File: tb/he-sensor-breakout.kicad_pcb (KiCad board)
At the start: 2 copper layers, 19 x 19 mm, 24 parts, among them J1 Conn_01x01_Pin, J10 Conn_01x01_Pin, J11 Conn_01x01_Pin, J12 Conn_01x01_Pin, J13 Conn_01x01_Pin, J14 Conn_01x01_Pin, J2 Conn_01x01_Pin, J3 Conn_01x01_Pin, J4 Conn_01x01_Pin, J5 Conn_01x01_Pin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

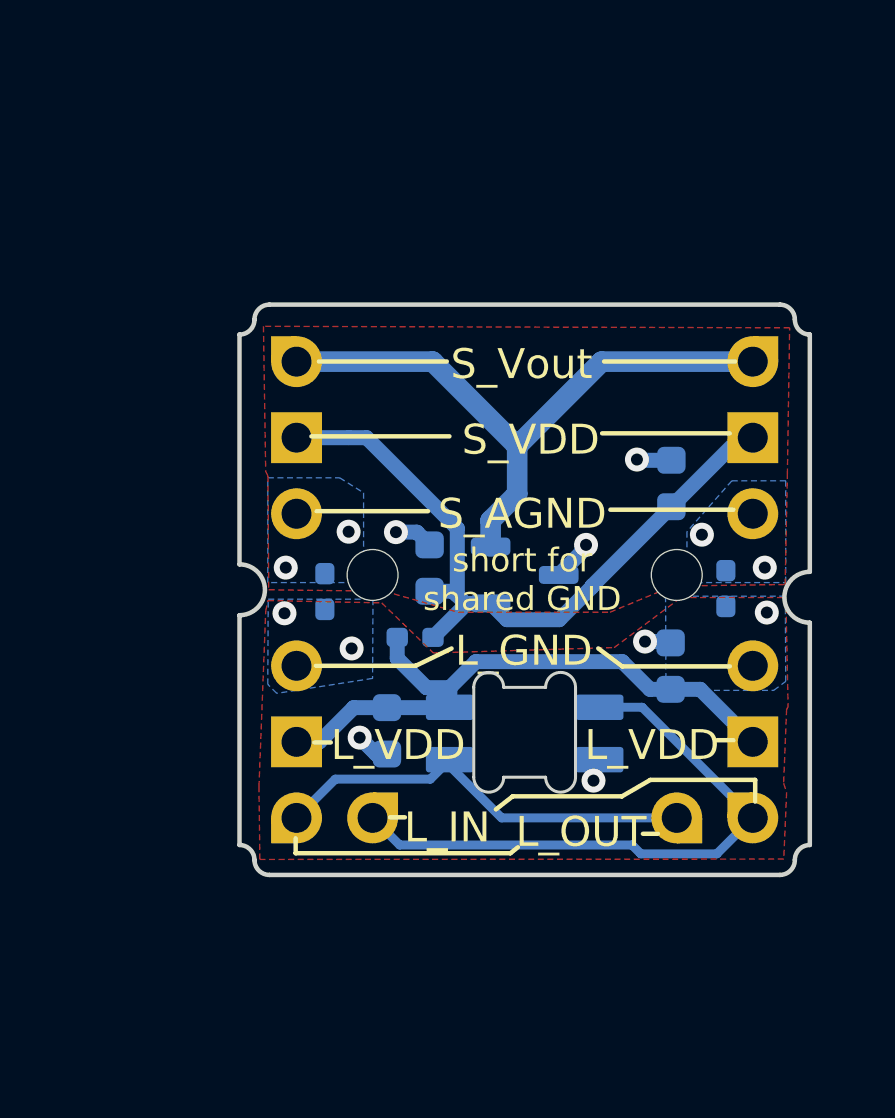
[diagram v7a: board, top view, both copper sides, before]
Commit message: fix screw hole
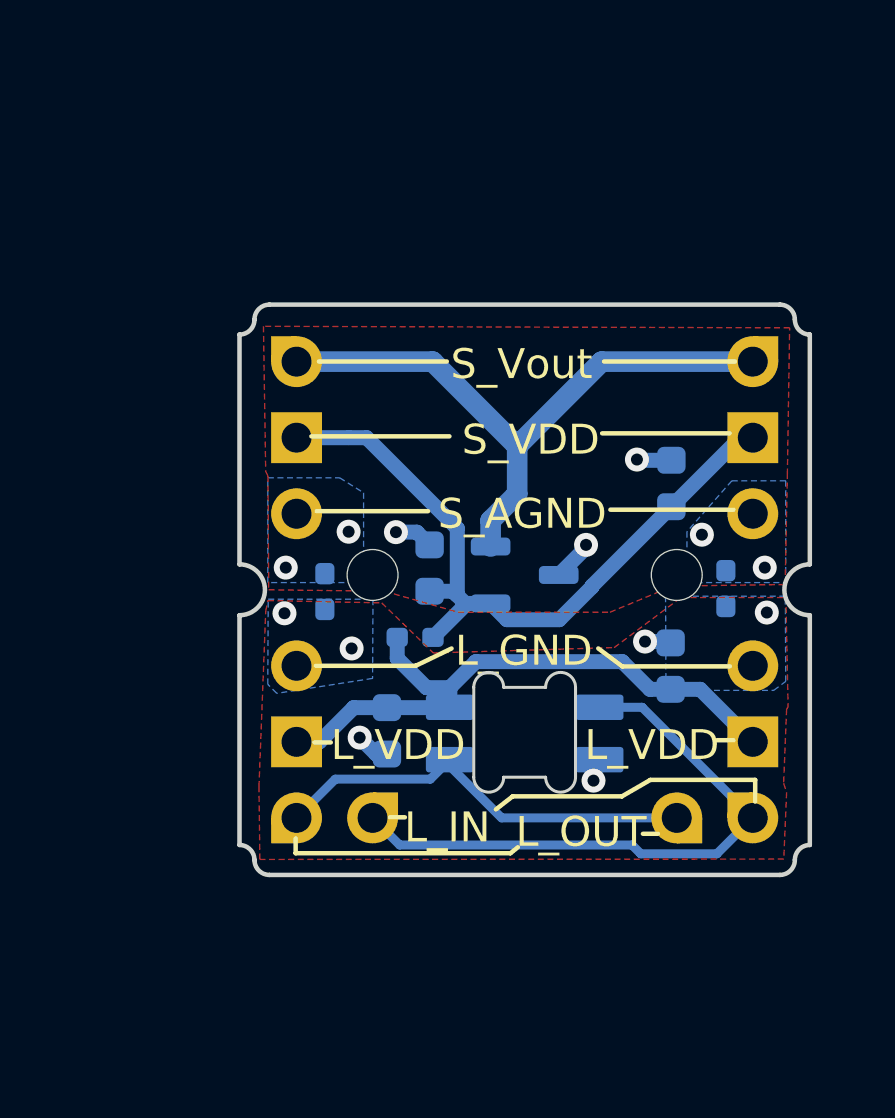
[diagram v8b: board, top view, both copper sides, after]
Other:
- outline, holes or cut-outs redrawn
- board text removed: "short for shared GND"
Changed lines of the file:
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@@
   (gr_arc (start 96.9 94.075) (mid 96.753553 94.428553) (end 96.4 94.575)
     (stroke (width 0.15) (type default)) (layer "Edge.Cuts"))
-  (gr_arc (start 115.45 104.2) (mid 114.6 103.35) (end 115.45 102.5)
+  (gr_arc (start 115.45 103.95) (mid 114.6 103.1) (end 115.45 102.25)
     (stroke (width 0.15) (type default)) (layer "Edge.Cuts"))
   (gr_line (start 96.4 94.575) (end 96.4 102.25)
@@
   (gr_line (start 114.45 112.625) (end 97.4 112.625)
     (stroke (width 0.15) (type default)) (layer "Edge.Cuts"))
-  (gr_line (start 115.45 104.2) (end 115.45 111.625)
+  (gr_line (start 115.45 103.95) (end 115.45 111.625)
     (stroke (width 0.15) (type default)) (layer "Edge.Cuts"))
-  (gr_line (start 115.45 94.575) (end 115.45 102.5)
+  (gr_line (start 115.45 94.575) (end 115.45 102.25)
     (stroke (width 0.15) (type default)) (layer "Edge.Cuts"))
   (gr_line (start 96.4 103.95) (end 96.4 111.625)
@@
     (effects (font (size 1 1) (thickness 0.15)) (justify left bottom))
   )
-  (gr_text "short for\nshared GND" (at 105.845 102.76) (layer "F.SilkS")
-    (effects (font (size 0.8 0.8) (thickness 0.15)))
-  )
   (gr_text "S_Vout" (at 103.45 96.15) (layer "F.SilkS")
